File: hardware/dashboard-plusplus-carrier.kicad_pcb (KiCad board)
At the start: 4 copper layers, 95 x 55 mm, 54 parts, among them J1 XT30U-M, J10a ESP32-DEVKIT-A, J10b ESP32-DEVKIT-B, J13 DEBUG, J14 TRIP + EN, J15 SPARE, J17 IGN + COOLANT, J3 TFT-ILI9488, J6 LDR + FUEL, J8 GPS_PADS, J9 HALL, Q1 IRFR9540N, U4 DPP_DCDC_MODULE

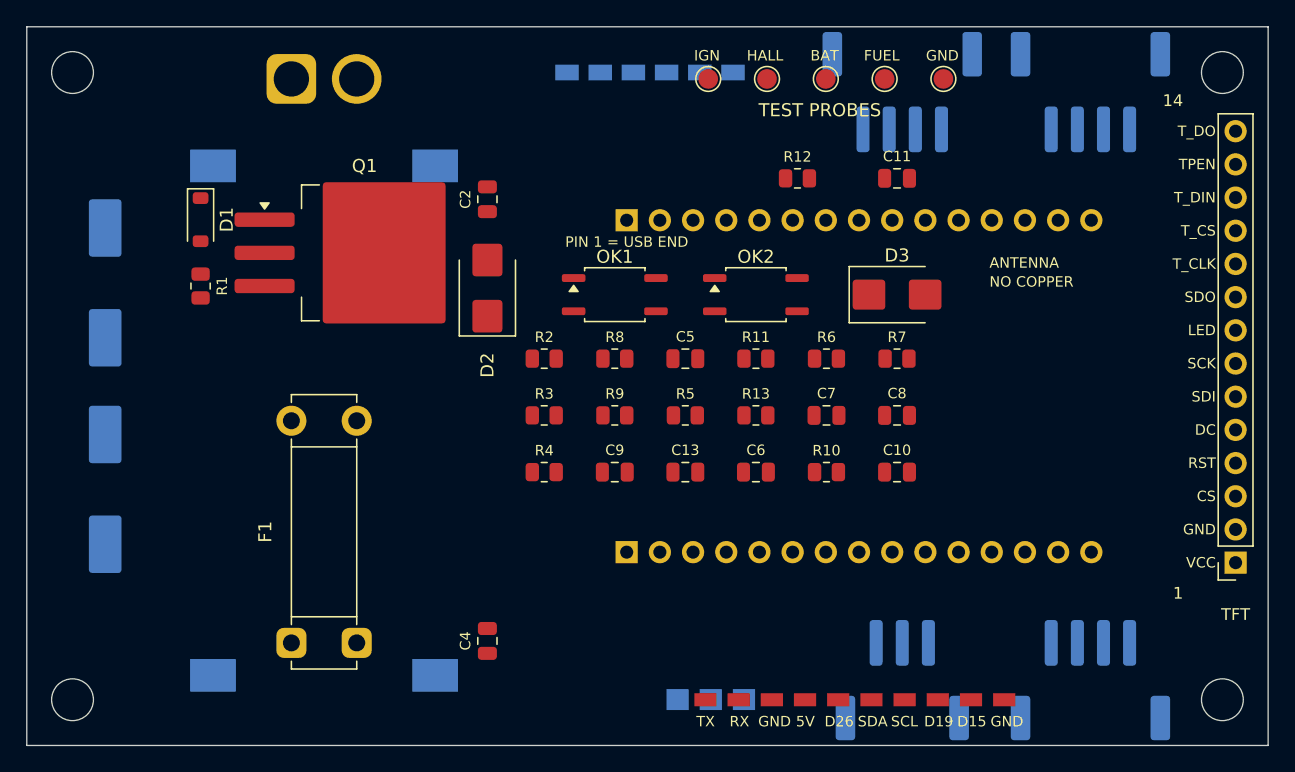
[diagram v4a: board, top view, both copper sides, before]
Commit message: Add A* autorouter, route the carrier on F.Cu and B.Cu
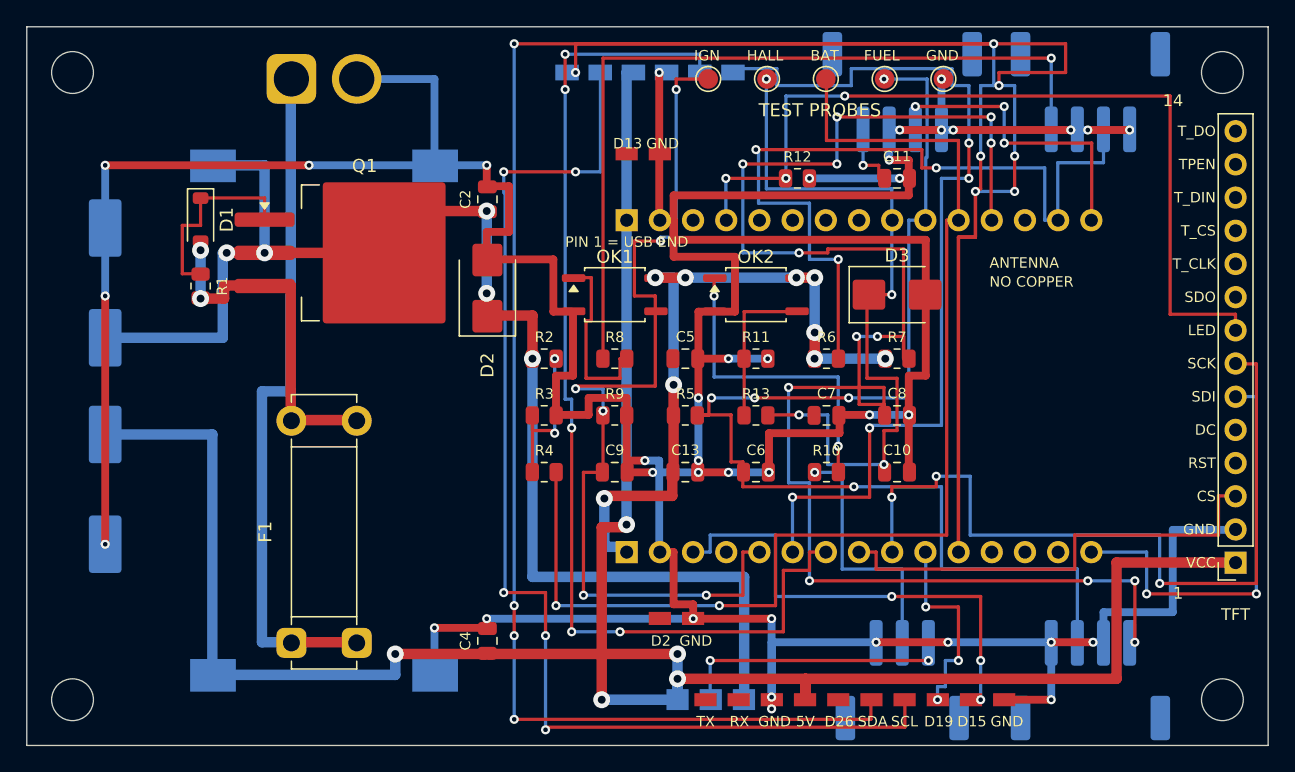
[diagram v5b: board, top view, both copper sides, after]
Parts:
- added J16: SPARE N, dpp:SPARE_N, F.Cu at (146.9, 87.2)
- added J18: SPARE S, dpp:SPARE_S, F.Cu at (149.4, 122.8)
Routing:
- net GND: track 0.00 -> 387.7 mm, vias 0 -> 38
- net SPARE_D21: track 0.00 -> 248.4 mm, vias 0 -> 11
- net V5: track 0.00 -> 178.7 mm, vias 0 -> 5
- net LDR_SNS: track 0.00 -> 127.9 mm, vias 0 -> 13
- net DC_12: track 0.00 -> 106.0 mm, vias 0 -> 5
- net FUEL_SNS: track 0.00 -> 92.5 mm, vias 0 -> 5
- net BAT_SNS: track 0.00 -> 91.0 mm, vias 0 -> 2
- net SPARE_D22: track 0.00 -> 90.5 mm, vias 0 -> 5
- net GPS_TX: track 0.00 -> 81.8 mm, vias 0 -> 5
- net IGN_SENSE: track 0.00 -> 72.5 mm, vias 0 -> 6
- net GPS_RX: track 0.00 -> 71.3 mm, vias 0 -> 4
- net TFT_BL: track 0.00 -> 66.2 mm, vias 0 -> 3
- net IGN_12: track 0.00 -> 62.6 mm, vias 0 -> 1
- net COOL_SNS: track 0.00 -> 60.9 mm, vias 0 -> 3
- net TFT_SCK: track 0.00 -> 60.1 mm, vias 0 -> 3
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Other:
- board text added: "D13"
- board text added: "D2"
- board text added: "J16 SPARE N (D13 GND) north of the near row,"
- board text added: "J18 SPARE S (D2 GND) south of the far row"

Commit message: Route short nets first inside a group, 11 unrouted to 7
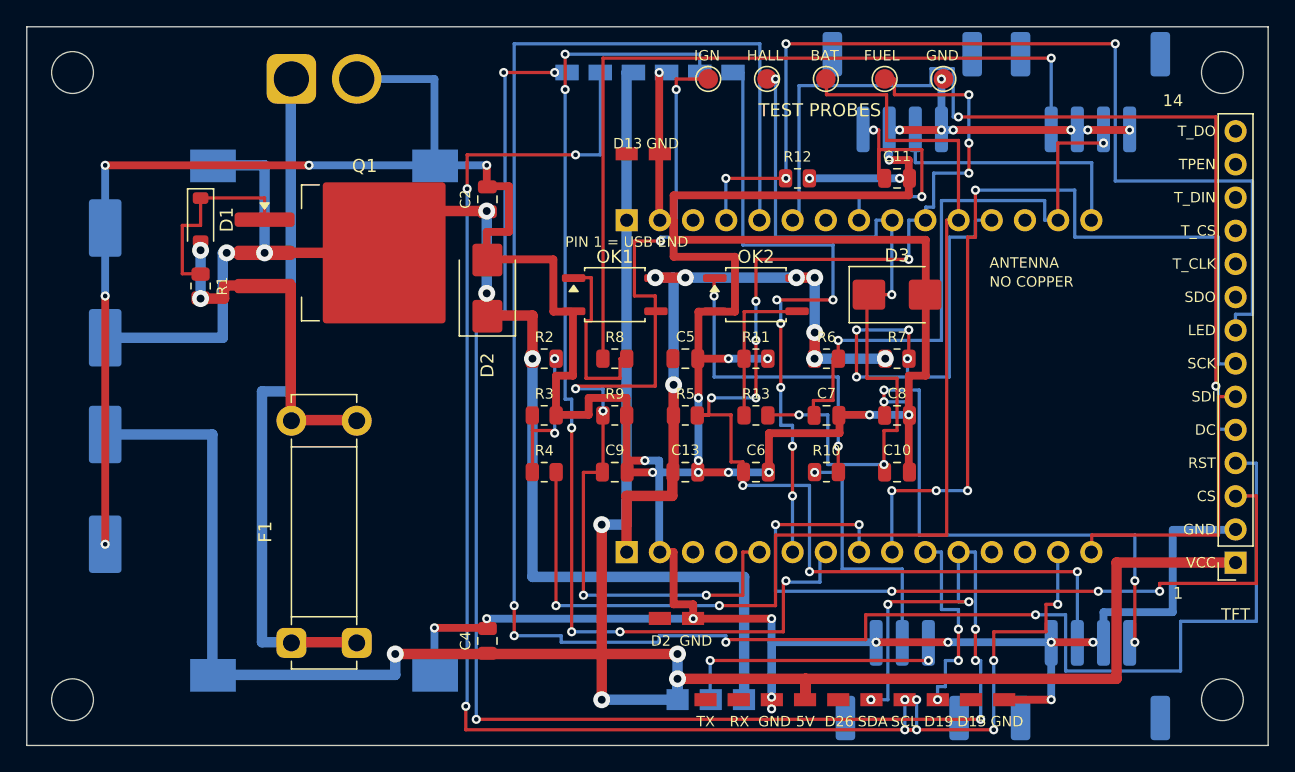
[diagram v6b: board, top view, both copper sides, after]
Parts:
- removed the C10 at (167.6, 111.6)
- removed the C7 at (162.2, 107.2)
- removed the C8 at (167.6, 107.2)
- removed the D1 at (114.3, 92.3)
- removed the H3 at (192.5, 129.0)
- removed the J10b at (146.9, 117.7)
- removed the J3 at (193.5, 118.5)
- removed the OK1 at (146.0, 98.0)
- removed the R10 at (162.2, 111.6)
- removed the R7 at (167.6, 102.9)
- added C1: 220u/50V, dpp:CP_Elec_10x12.5, B.Cu at (107.0, 97.1)
- added C11: 100n, dpp:C_0805_2012Metric, F.Cu at (167.6, 89.1)
- added F1: 5x20 2A, dpp:Fuseholder_Clip-5x20mm_Littelfuse_521_Lateral_P17.00x5.00mm_D1.30mm_Horizontal, F.Cu at (121.2, 124.7)
- added J13: DEBUG, dpp:DEBUG, F.Cu at (152.9, 129.0)
- added J15: SPARE, dpp:SPARE, F.Cu at (163.1, 129.0)
- added J17: IGN + COOLANT, dpp:JST_PH_S4B-PH-SM4-TB_1x04-1MP_P2.00mm_Horizontal, B.Cu at (182.4, 82.5)
- added J18: SPARE S, dpp:SPARE_S, F.Cu at (149.4, 122.8)
- added J6: LDR + FUEL, dpp:JST_PH_S4B-PH-SM4-TB_1x04-1MP_P2.00mm_Horizontal, B.Cu at (182.4, 127.5)
- added R12: 10k, dpp:R_0805_2012Metric, F.Cu at (160.0, 89.1)
- added TP3: BAT_SNS, dpp:TestPoint_Pad_D1.5mm, F.Cu at (162.2, 81.5)
- C10: renamed from J15; value SPARE -> 100n; footprint dpp:SPARE -> dpp:C_0805_2012Metric
- C7: renamed from D3; value P6SMB6V2A -> 100n; footprint dpp:D_SMB -> dpp:C_0805_2012Metric
- C8: renamed from J13; value DEBUG -> 100n; footprint dpp:DEBUG -> dpp:C_0805_2012Metric
- D1: renamed from C1; value 220u/50V -> BZT52C15V; footprint dpp:CP_Elec_10x12.5 -> dpp:D_SOD-123; moved to F.Cu
- D3: renamed from TP3; value BAT_SNS -> P6SMB6V2A; footprint dpp:TestPoint_Pad_D1.5mm -> dpp:D_SMB
- H3: renamed from F1; value 5x20 2A -> MOUNT; footprint dpp:Fuseholder_Clip-5x20mm_Littelfuse_521_Lateral_P17.00x5.00mm_D1.30mm_Horizontal -> dpp:MOUNT
- J10b: renamed from J17; value IGN + COOLANT -> ESP32-DEVKIT-B; footprint dpp:JST_PH_S4B-PH-SM4-TB_1x04-1MP_P2.00mm_Horizontal -> dpp:PinSocket_1x15_P2.54mm_Vertical
- J3: renamed from J6; value LDR + FUEL -> TFT-ILI9488; footprint dpp:JST_PH_S4B-PH-SM4-TB_1x04-1MP_P2.00mm_Horizontal -> dpp:PinSocket_1x14_P2.54mm_Vertical; moved to F.Cu
- OK1: renamed from J18; value SPARE S -> EL357N-B; footprint dpp:SPARE_S -> dpp:SO-4_4.4x3.9mm_P2.54mm
- R10: renamed from C11; value 100n -> 1k; footprint dpp:C_0805_2012Metric -> dpp:R_0805_2012Metric
- moved H3 71.4 mm to (192.5, 129.0), turned to 0 degrees
- moved J10b 50.0 mm to (146.9, 117.7), turned to 270 degrees
- moved C8 26.2 mm to (167.6, 107.2)
- moved OK1 25.0 mm to (146.0, 98.0)
- moved R10 23.1 mm to (162.2, 111.6)
- moved C10 18.0 mm to (167.6, 111.6)
- moved D3 17.4 mm to (167.6, 98.0)
- moved R7 15.8 mm to (167.6, 102.9)
- moved J3 14.3 mm to (193.5, 118.5)
- moved C7 10.7 mm to (162.2, 107.2)
- moved D1 8.76 mm to (114.3, 92.3), turned to 270 degrees
- renumbered R12 to R7
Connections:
- C10 pad 1: SPARE_D26 -> HALL
- C10 pad 2: SPARE_D21 -> GND
- C7 pad 1: HALL -> COOL_SNS
- C8 pad 1: DBG_TX -> LDR_SNS
- C8 pad 2: DBG_RX -> GND
- D1 pad 1: DC_12 -> MOS_G
- D1 pad 2: GND -> DC_F
- D3 pad 1: BAT_SNS -> HALL
- H3 pad 1: DC_IN -> (no net)
- J10b pad 1: IGN_12 -> V3V3
- J10b pad 3: COOL_SNS -> SPARE_D15
- J10b pad 4: GND -> SPARE_D2
- J3 pad 1: LDR_SNS -> V5
- J3 pad 3: FUEL_SNS -> TFT_CS
- J3 pad 4: GND -> TFT_RST
- OK1 pad 1: SPARE_D2 -> IGN_LED
- R10 pad 1: TRIP_BTN -> HALL_SIG
- R10 pad 2: GND -> HALL_LED
- R7 pad 1: TFT_BL -> V3V3
- R7 pad 2: GND -> LDR_SNS
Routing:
- net TFT_RST: track 0.00 -> 159.6 mm, vias 0 -> 4
- net SPARE_D21: track 248.4 -> 129.0 mm, vias 11 -> 9
- net TFT_DC: track 0.00 -> 72.9 mm, vias 0 -> 2
- net LDR_SNS: track 127.9 -> 78.5 mm, vias 13 -> 8
- net SPARE_D15: track 36.5 -> 0.00 mm, vias 3 -> 0
- net SPARE_D22: track 90.5 -> 125.6 mm, vias 5 -> 10
- net TFT_CS: track 35.5 -> 59.1 mm, vias 0 -> 5
- net GPS_RX: track 71.3 -> 49.8 mm, vias 4 -> 6
- net TRIP_BTN: track 5.40 -> 21.3 mm, vias 1 -> 2
- net COOL_SNS: track 60.9 -> 46.7 mm, vias 3 -> 2
- net TFT_BL: track 66.2 -> 76.8 mm, vias 3 -> 4
- net TFT_MOSI: track 32.3 -> 22.7 mm, vias 2 -> 0
- net TFT_SCK: track 60.1 -> 67.1 mm, vias 3 -> 4
- net FUEL_SNS: track 92.5 -> 98.8 mm, vias 5 -> 11
- net EN: track 23.9 -> 20.4 mm, vias 3 -> 0
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
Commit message: Reclassify V3V3 to a Ref class, all functional nets route
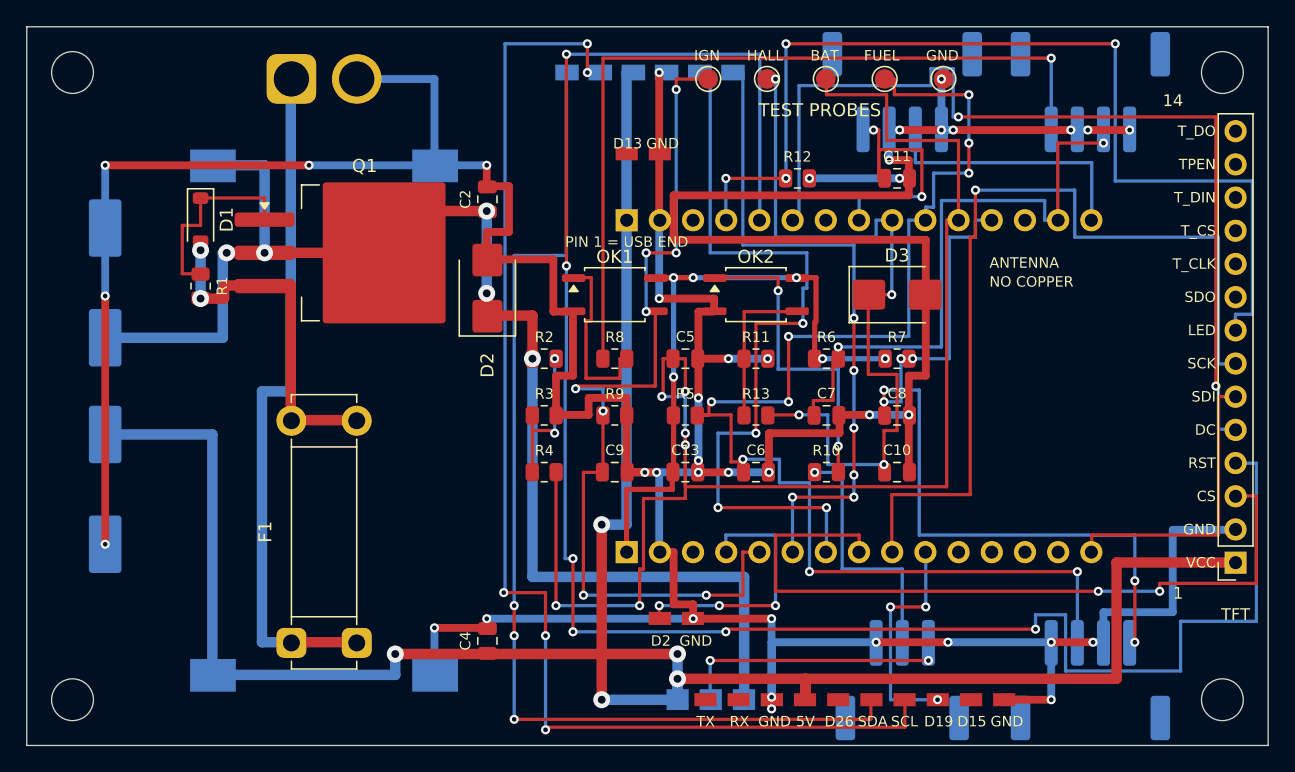
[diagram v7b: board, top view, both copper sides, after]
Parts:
- removed the D3 at (167.6, 98.0)
- removed the F1 at (121.2, 124.7)
- removed the H2 at (192.5, 81.0)
- removed the H3 at (192.5, 129.0)
- removed the J13 at (152.9, 129.0)
- removed the J15 at (163.1, 129.0)
- removed the J16 at (146.9, 87.2)
- removed the J18 at (149.4, 122.8)
- removed the J8 at (142.3, 81.0)
- removed the JP1 at (150.8, 129.0)
- removed the R12 at (160.0, 89.1)
- removed the R13 at (156.8, 107.2)
- removed the TP1 at (153.2, 81.5)
- removed the TP5 at (171.2, 81.5)
- added C4: 100n, dpp:C_0805_2012Metric, F.Cu at (136.2, 124.5)
- added C7: 100n, dpp:C_0805_2012Metric, F.Cu at (162.2, 107.2)
- added C9: 100n, dpp:C_0805_2012Metric, F.Cu at (146.0, 111.6)
- added D1: BZT52C15V, dpp:D_SOD-123, F.Cu at (114.3, 92.3)
- added J10a: ESP32-DEVKIT-A, dpp:PinSocket_1x15_P2.54mm_Vertical, B.Cu at (146.9, 92.3)
- added J10b: ESP32-DEVKIT-B, dpp:PinSocket_1x15_P2.54mm_Vertical, B.Cu at (146.9, 117.7)
- added J3: TFT-ILI9488, dpp:PinSocket_1x14_P2.54mm_Vertical, F.Cu at (193.5, 118.5)
- added J6: LDR + FUEL, dpp:JST_PH_S4B-PH-SM4-TB_1x04-1MP_P2.00mm_Horizontal, B.Cu at (182.4, 127.5)
- added R2: 47k, dpp:R_0805_2012Metric, F.Cu at (140.6, 102.9)
- added R3: 10k, dpp:R_0805_2012Metric, F.Cu at (140.6, 107.2)
- added R4: 1k, dpp:R_0805_2012Metric, F.Cu at (140.6, 111.6)
- added R8: 1k, dpp:R_0805_2012Metric, F.Cu at (146.0, 102.9)
- added R9: 10k, dpp:R_0805_2012Metric, F.Cu at (146.0, 107.2)
- added U4: DPP_DCDC_MODULE, dpp:DPP_DCDC_MODULE, B.Cu at (123.8, 107.6)
- C11: renamed from R2; value 47k -> 100n; footprint dpp:R_0805_2012Metric -> dpp:C_0805_2012Metric
- D3: renamed from C4; value 100n -> P6SMB6V2A; footprint dpp:C_0805_2012Metric -> dpp:D_SMB
- F1: renamed from J6; value LDR + FUEL -> 5x20 2A; footprint dpp:JST_PH_S4B-PH-SM4-TB_1x04-1MP_P2.00mm_Horizontal -> dpp:Fuseholder_Clip-5x20mm_Littelfuse_521_Lateral_P17.00x5.00mm_D1.30mm_Horizontal; moved to F.Cu
- H2: renamed from J3; value TFT-ILI9488 -> MOUNT; footprint dpp:PinSocket_1x14_P2.54mm_Vertical -> dpp:MOUNT
- H3: renamed from U4; value DPP_DCDC_MODULE -> MOUNT; footprint dpp:DPP_DCDC_MODULE -> dpp:MOUNT; moved to F.Cu
- J13: renamed from R4; value 1k -> DEBUG; footprint dpp:R_0805_2012Metric -> dpp:DEBUG
- J15: renamed from R8; value 1k -> SPARE; footprint dpp:R_0805_2012Metric -> dpp:SPARE
- J16: renamed from R9; value 10k -> SPARE N; footprint dpp:R_0805_2012Metric -> dpp:SPARE_N
- J18: renamed from C9; value 100n -> SPARE S; footprint dpp:C_0805_2012Metric -> dpp:SPARE_S
- J8: renamed from J10a; value ESP32-DEVKIT-A -> GPS_PADS; footprint dpp:PinSocket_1x15_P2.54mm_Vertical -> dpp:GPS_PADS
- JP1: renamed from J10b; value ESP32-DEVKIT-B -> JP1_PADS_3; footprint dpp:PinSocket_1x15_P2.54mm_Vertical -> dpp:JP1_PADS_3
- R13: renamed from D1; value BZT52C15V -> 1k; footprint dpp:D_SOD-123 -> dpp:R_0805_2012Metric
- TP1: renamed from C7; value 100n -> IGN_SENSE; footprint dpp:C_0805_2012Metric -> dpp:TestPoint_Pad_D1.5mm
- TP5: renamed from C11; value 100n -> GND; footprint dpp:C_0805_2012Metric -> dpp:TestPoint_Pad_D1.5mm
- moved H3 72.0 mm to (192.5, 129.0)
- moved F1 61.2 mm to (121.2, 124.7), turned to 90 degrees
- moved R13 45.1 mm to (156.8, 107.2), turned to 0 degrees
- moved D3 41.0 mm to (167.6, 98.0), turned to 0 degrees
- moved H2 37.5 mm to (192.5, 81.0), turned to 0 degrees
- moved J15 31.2 mm to (163.1, 129.0)
- moved C11 30.3 mm to (167.6, 89.1)
- moved TP1 27.3 mm to (153.2, 81.5)
- moved R12 26.5 mm to (160.0, 89.1)
- moved J13 21.3 mm to (152.9, 129.0)
- moved J16 20.0 mm to (146.9, 87.2)
- moved J8 12.2 mm to (142.3, 81.0), turned to 0 degrees
- moved JP1 11.9 mm to (150.8, 129.0), turned to 0 degrees
- moved J18 11.7 mm to (149.4, 122.8)
- moved TP5 8.40 mm to (171.2, 81.5)
- renumbered R3 to R12
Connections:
- C11 pad 1: DC_12 -> TRIP_BTN
- C11 pad 2: BAT_DIV -> GND
- D3 pad 1: V5 -> HALL
- F1 pad 1: LDR_SNS -> DC_IN
- F1 pad 2: GND -> DC_F
- H2 pad 1: V5 -> (no net)
- H3 pad 1: DC_12 -> (no net)
- J13 pad 1: BAT_DIV -> DBG_TX
- J13 pad 2: BAT_SNS -> DBG_RX
- J15 pad 1: IGN_12 -> SPARE_D26
- J15 pad 2: IGN_LED -> SPARE_D21
- J16 pad 1: IGN_SENSE -> SPARE_D13
- J18 pad 1: IGN_SENSE -> SPARE_D2
- J8 pad 1: V5 -> SPARE_D21
- J8 pad 2: GND -> SPARE_D22
- J8 pad 3: SPARE_D13 -> V5
- J8 pad 4: TFT_BL -> GND
- J8 pad 5: TFT_RST -> GPS_TX
- J8 pad 6: TFT_DC -> GPS_RX
- JP1 pad 1: V3V3 -> V5
- JP1 pad 2: GND -> HALL_VCC
- JP1 pad 3: SPARE_D15 -> DC_12
- R12 pad 1: BAT_DIV -> TFT_BL
- R13 pad 1: MOS_G -> HALL_OUT
- R13 pad 2: DC_F -> HALL
- TP1 pad 1: COOL_SNS -> IGN_SENSE
- TP5 pad 1: TRIP_BTN -> GND
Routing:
- net SPARE_D21: track 129.0 -> 82.1 mm, vias 9 -> 3
- net SPARE_D22: track 125.6 -> 94.9 mm, vias 10 -> 5
- net BAT_SNS: track 91.0 -> 114.1 mm, vias 2 -> 6
- net GPS_TX: track 81.9 -> 59.9 mm, vias 6 -> 4
- net SPARE_D2: track 0.00 -> 20.2 mm, vias 0 -> 3
- net LDR_SNS: track 78.5 -> 63.5 mm, vias 8 -> 6
- net TFT_RST: track 159.6 -> 147.5 mm, vias 4 -> 6
- net GND: track 387.7 -> 382.7 mm, vias 38 -> 39
- net SPARE_D19: track 15.3 -> 17.5 mm
- net FUEL_SNS: track 98.8 -> 100.8 mm, vias 11 -> 9
- net IGN_SENSE: track 72.5 -> 70.7 mm, vias 6 -> 8
- net TFT_CS: track 59.1 -> 57.5 mm, vias 5 -> 2
- net GPS_RX: track 49.8 -> 50.6 mm
- net V3V3: vias 8 -> 6
- net TFT_SCK: vias 4 -> 1
